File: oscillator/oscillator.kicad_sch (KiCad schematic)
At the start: 37 parts, among them J1 Output, J2 Output, J3 Triangle Output, J4 Saw Output, J5 Pulse Output, J6 Frequency CV Input, J7 PWM CV Input, SW1 LFO Switch, U1 AS3340-custom, U2 TL074

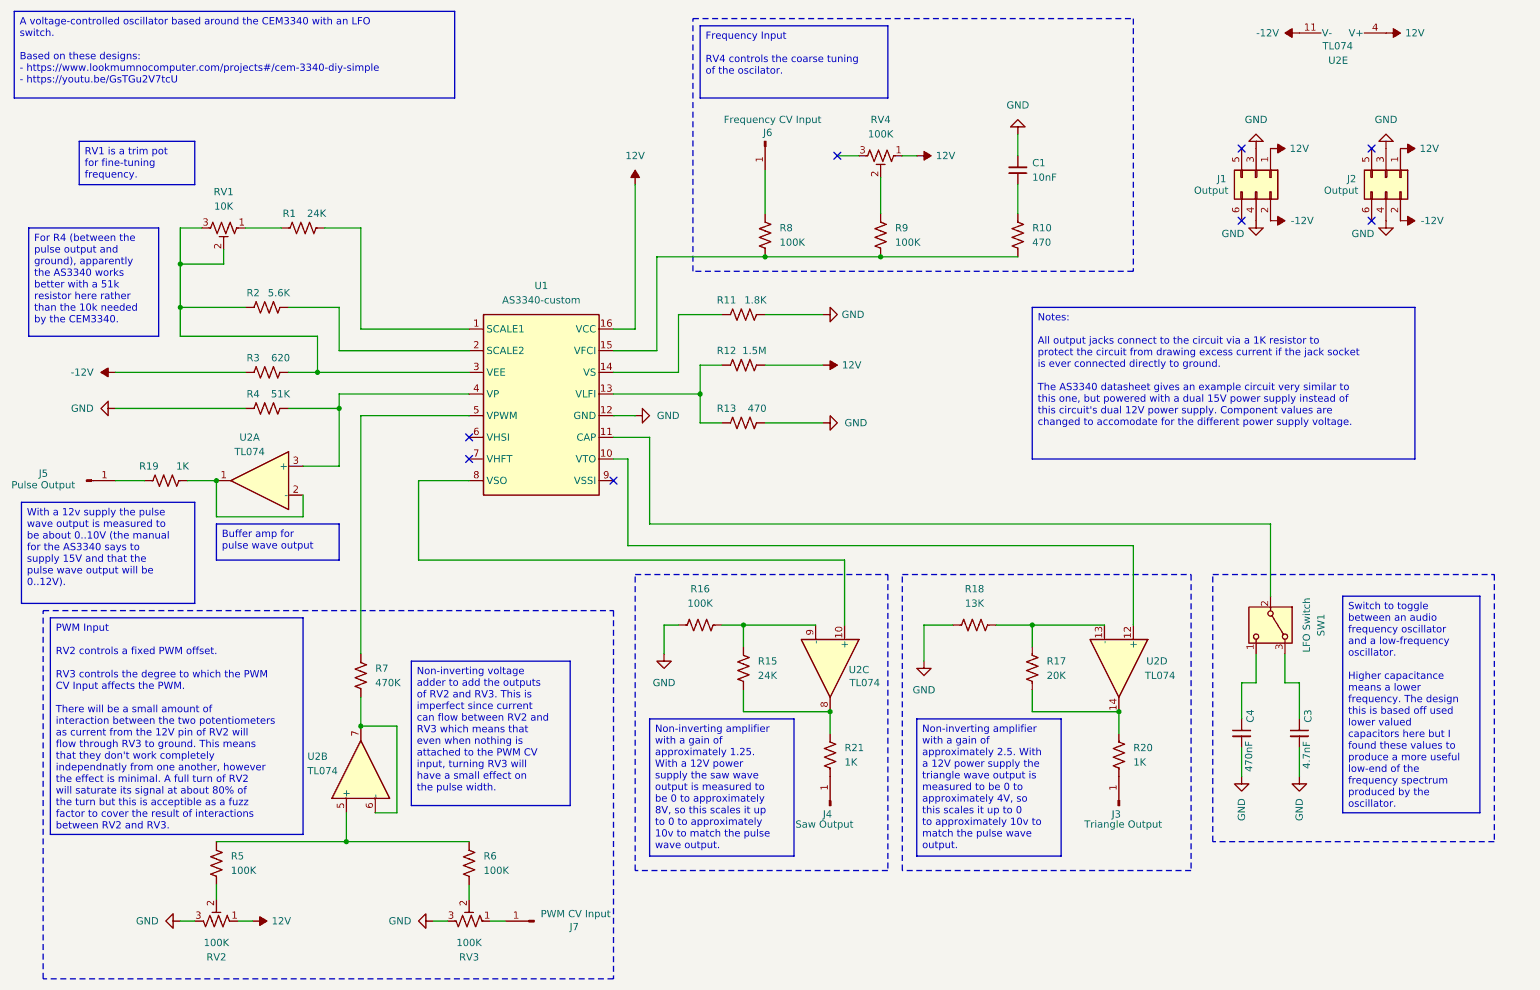
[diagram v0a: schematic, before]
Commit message: Redesign oscillator
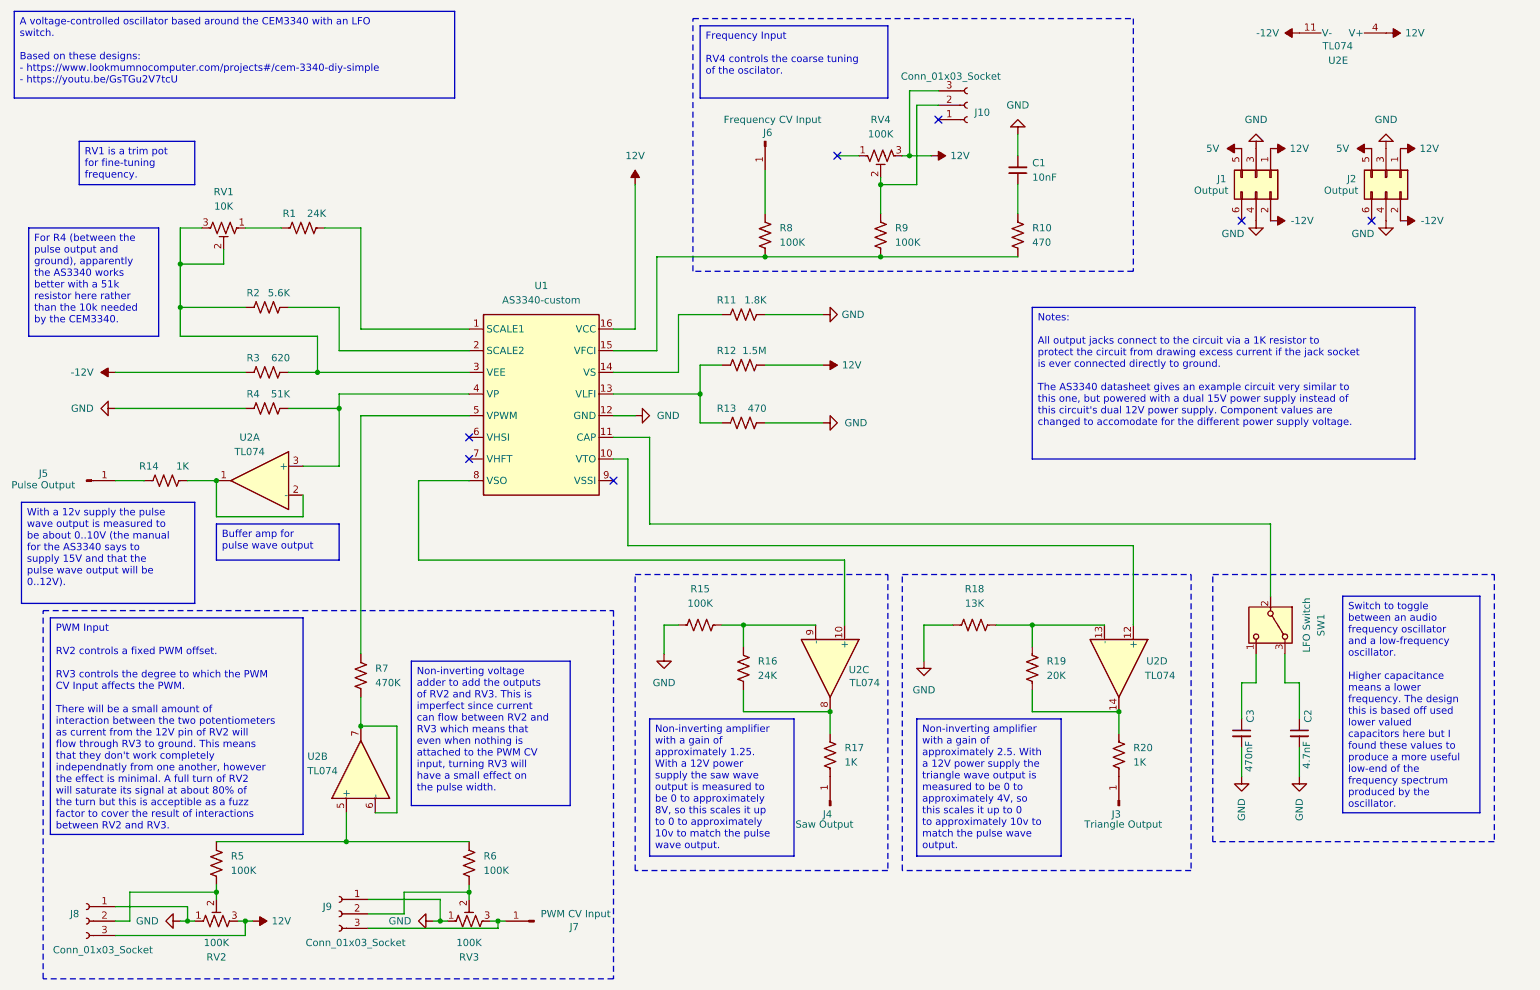
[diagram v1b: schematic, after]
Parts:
- added J10, J8, J9: Conn_01x03_Socket, modular2:pot, symbol Connector:Conn_01x03_Socket
- renumbered C3 to C2, C4 to C3, R19 to R14, R16 to R15, R15 to R16, R21 to R17, R17 to R19
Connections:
- net 12V: now also RV2.3, RV4.3, J10.3 (Pin_3), J8.3 (Pin_3); no longer RV2.1, RV4.1
- net GND: now also RV2.1, RV3.1, J8.1 (Pin_1), J9.1 (Pin_1); no longer RV2.3, RV3.3
- net at R5.2, RV2.2: now also J8.2 (Pin_2)
- net 5V: now reaches J2.5 (Pin_5)
- net 5V: now also J1.5 (Pin_5)
- net at R9.1, RV4.2: now also J10.2 (Pin_2)
- net at R6.2, RV3.2: now also J9.2 (Pin_2)
- net at J7.1 (Pin_1): now also RV3.3, J9.3 (Pin_3); no longer RV3.1
- no-connect marks 8 -> 7
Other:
- moved on the sheet: RV2, RV3, RV4

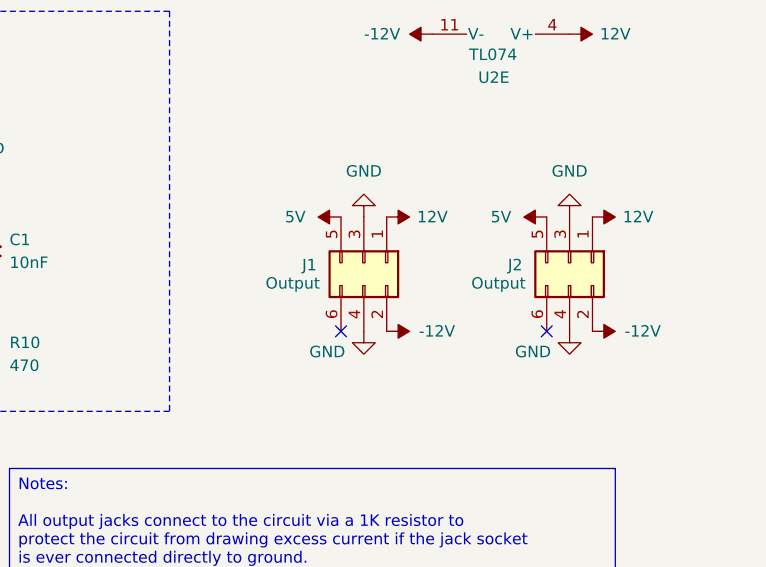
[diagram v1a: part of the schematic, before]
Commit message: Add mixer and power expander
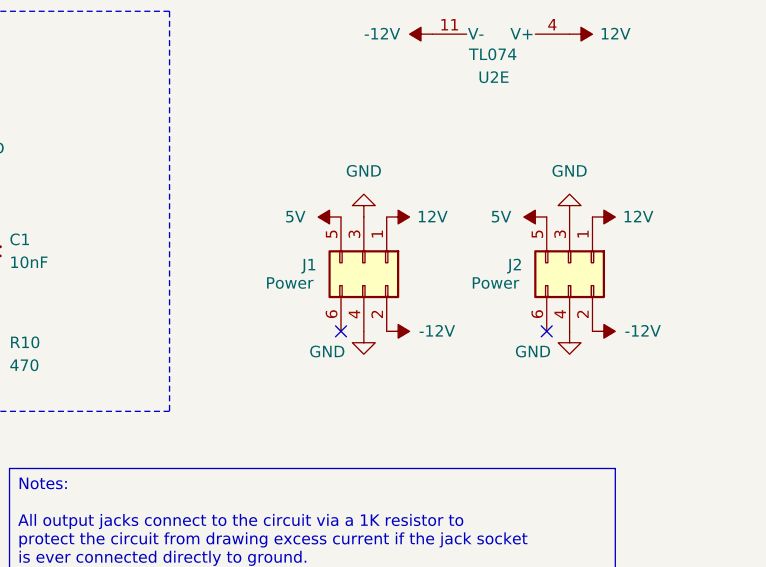
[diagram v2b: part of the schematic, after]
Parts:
- J1, J2: value Output -> Power
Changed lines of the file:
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@@
 			)
 		)
-		(property "Value" "Output"
+		(property "Value" "Power"
 			(at 248.158 45.466 90)
 			(effects
@@
 			)
 		)
-		(property "Value" "Output"
+		(property "Value" "Power"
 			(at 225.298 45.466 90)
 			(effects

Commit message: Various improvements
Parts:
- added C4, C5, C6: 100nf, Capacitor_THT:C_Disc_D4.3mm_W1.9mm_P5.00mm, symbol Device:C_Small
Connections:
- net -12V: now also C4.2
- net 12V: now also C5.1, C6.1
- net GND: now also C4.1, C5.2, C6.2

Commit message: Various fixes
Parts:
- added J11: Power, Connector_IDC:IDC-Header_2x03_P2.54mm_Vertical, symbol Connector_Generic:Conn_02x03_Odd_Even
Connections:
- net -12V: now also J11.2 (Pin_2)
- net 12V: now also J11.1 (Pin_1)
- net 5V: now also J11.5 (Pin_5)
- net GND: now also J11.3 (Pin_3), J11.4 (Pin_4)
- no-connect marks 7 -> 8
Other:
- moved on the sheet: J1, J2

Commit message: Various improvements
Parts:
- added C7, C8: 100nf, Capacitor_THT:C_Disc_D4.3mm_W1.9mm_P5.00mm, symbol Device:C_Small
- added J12: Soft Sync, modular2:banana-jack, symbol Connector:Conn_01x01_Pin
- added J13: Hard Sync, modular2:banana-jack, symbol Connector:Conn_01x01_Pin
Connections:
- net at U1.6 (VHSI): now also C8.2
- net at U1.9 (VSSI): now also C7.2
- new net: C8.1, J13.1 (Pin_1)
- new net: C7.1, J12.1 (Pin_1)
- no-connect marks 8 -> 6
